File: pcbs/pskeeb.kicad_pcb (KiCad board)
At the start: 2 copper layers, 136.5 x 99.5 mm, 29 parts, among them K11 KEYSW, K12 KEYSW, K13 KEYSW, K14 KEYSW, K15 KEYSW, K21 KEYSW, K22 KEYSW, K23 KEYSW, K24 KEYSW, K25 KEYSW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

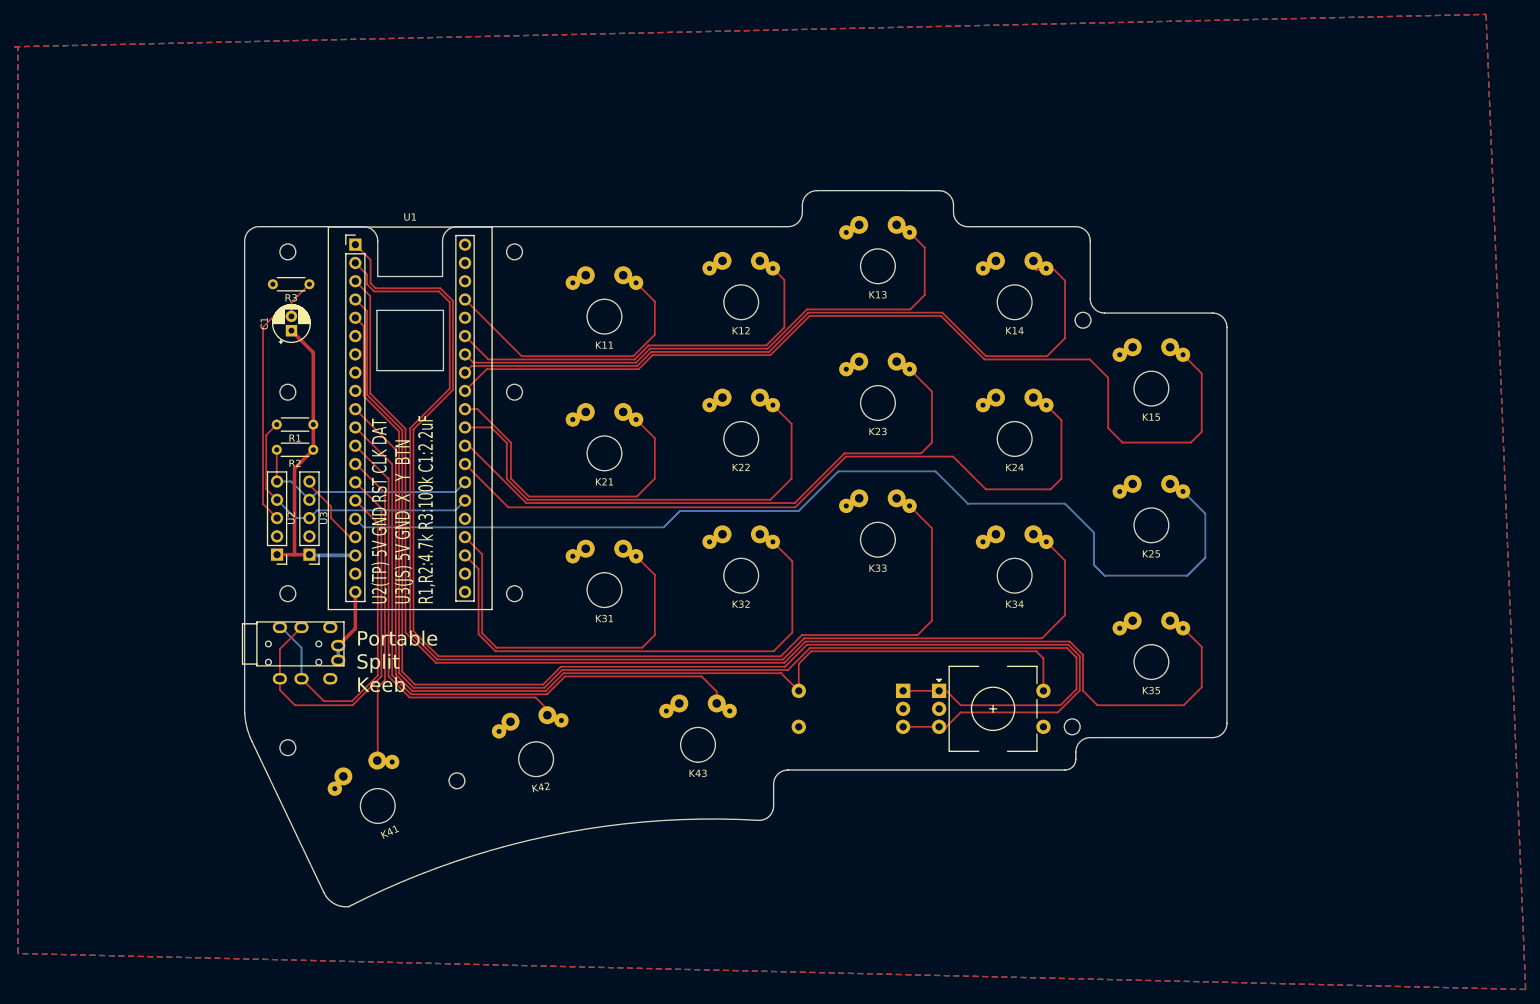
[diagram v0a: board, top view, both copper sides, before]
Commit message: fix: bigger resistor / ec11 share holes / usb fit
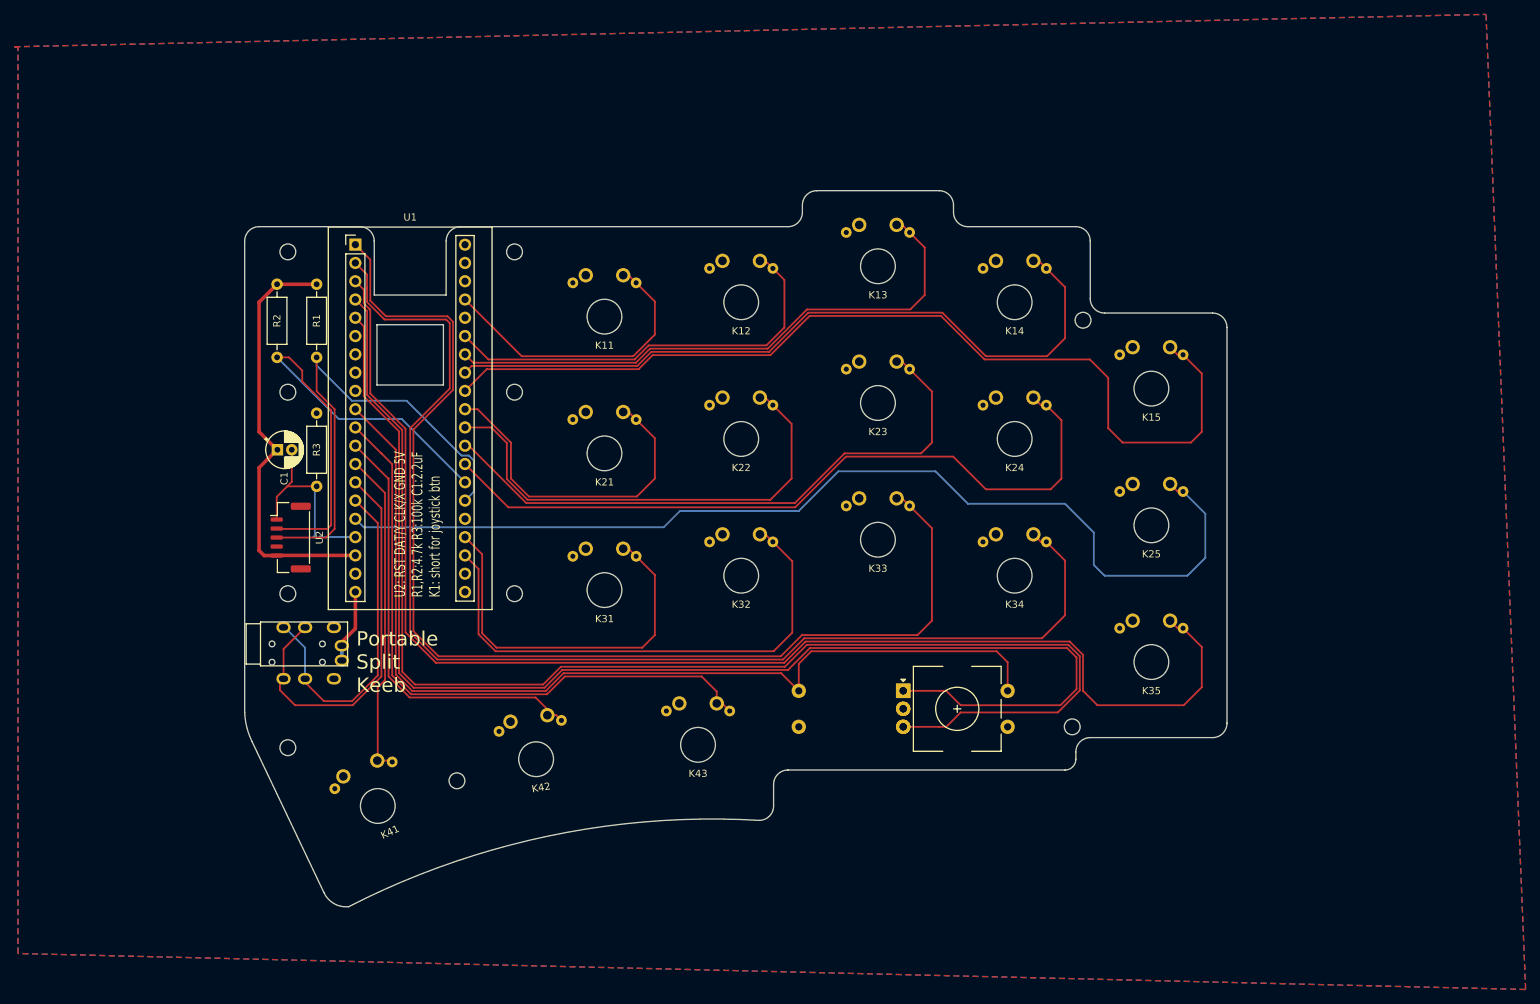
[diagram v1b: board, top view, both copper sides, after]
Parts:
- removed U3: JoyStick, Connector_PinHeader_2.54mm:PinHeader_1x05_P2.54mm_Vertical
- added K1: KEYSW, Resistor_SMD:R_0201_0603Metric_Pad0.64x0.40mm_HandSolder, B.Cu at (88.2, 97.6)
- R1, R2, R3: footprint Resistor_THT:R_Axial_DIN0204_L3.6mm_D1.6mm_P5.08mm_Horizontal -> Resistor_THT:R_Axial_DIN0207_L6.3mm_D2.5mm_P10.16mm_Horizontal
- U2: value PS/2_Trackpoint -> trackpoint/joystick; footprint Connector_PinHeader_2.54mm:PinHeader_1x05_P2.54mm_Vertical -> Connector_JST:JST_GH_BM05B-GHS-TBT_1x05-1MP_P1.25mm_Vertical
- moved R3 28.1 mm to (88.0, 90.6), turned to 90 degrees
- moved R2 23.5 mm to (82.5, 62.5), turned to -90 degrees
- moved R1 19.5 mm to (88.0, 62.5), turned to -90 degrees
- moved C1 16.7 mm to (82.5, 85.5), turned to 0 degrees
- moved ENC1 4.98 mm to (177.0, 121.5)
- moved U2 3.04 mm to (84.4, 97.7), turned to -90 degrees
- moved TRRS1 0.50 mm to (80.2, 115.0)
- moved TRRS2 0.50 mm to (80.2, 112.5)
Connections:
- C1 pad 2: Net-(C1-Pad2) -> /RST/BTN
- R1 pad 2: /joystick_x -> /CLK/X
- R2 pad 2: /joystick_y -> /DAT/Y
- R3 pad 1: Net-(C1-Pad2) -> /RST/BTN
- U1 pad 26: /joystick_x -> /CLK/X
- U1 pad 27: /joystick_y -> /DAT/Y
- U2 pad 1: +5V -> /RST/BTN
- U2 pad 2: GND -> /DAT/Y
- U2 pad 3: Net-(C1-Pad2) -> /CLK/X
- U2 pad 4: /joystick_x -> GND
- U2 pad 5: /joystick_y -> +5V
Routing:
- net /DAT/Y: track 0.00 -> 68.5 mm
- net /CLK/X: track 0.00 -> 67.9 mm
- net /joystick_x: track 39.9 -> 0.00 mm
- net Net-(C1-Pad2): track 37.4 -> 0.00 mm
- net /joystick_y: track 32.6 -> 0.00 mm
- net /RST/BTN: track 0.00 -> 21.8 mm
- net +5V: track 44.4 -> 59.3 mm
- net /joystick_btn: track 10.8 -> 4.82 mm
- net /k44: track 141.6 -> 136.3 mm
- net /k35: track 182.2 -> 184.7 mm
- net /k42: track 58.9 -> 61.2 mm
- net /k32: track 71.1 -> 73.3 mm
- net /k23: track 83.1 -> 85.4 mm
- net /k31: track 51.9 -> 54.2 mm
- net /k21: track 44.6 -> 46.9 mm
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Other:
- outline, holes or cut-outs redrawn
- board text added: "U2: RST DAT/Y CLK/X GND 5V R1,R2:4.7k R3:100k C1:2.2uF K1: short for joystick btn"
- board text removed: "U2(TP) 5V GND RST CLK DAT U3(JS) 5V GND X Y BTN R1,R2:4.7k R3:100k C1:2.2uF"
